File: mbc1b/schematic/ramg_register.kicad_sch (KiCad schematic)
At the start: 8 parts

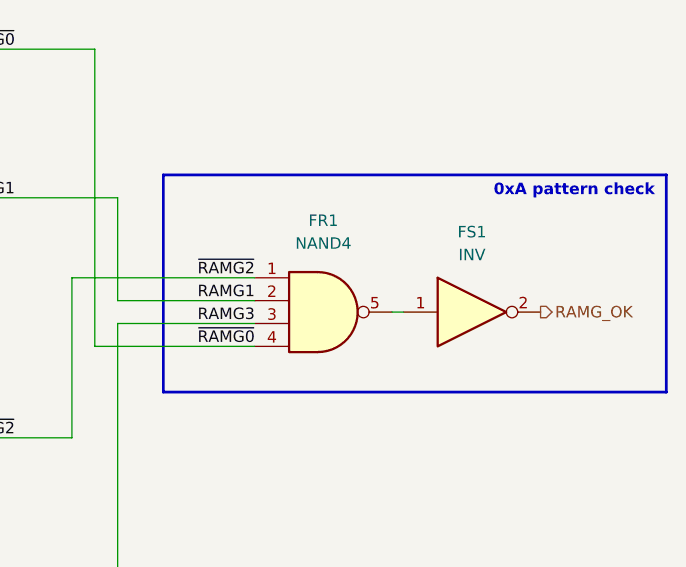
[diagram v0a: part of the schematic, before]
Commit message: Update MBC1B schematic with latest kingfish compatibility
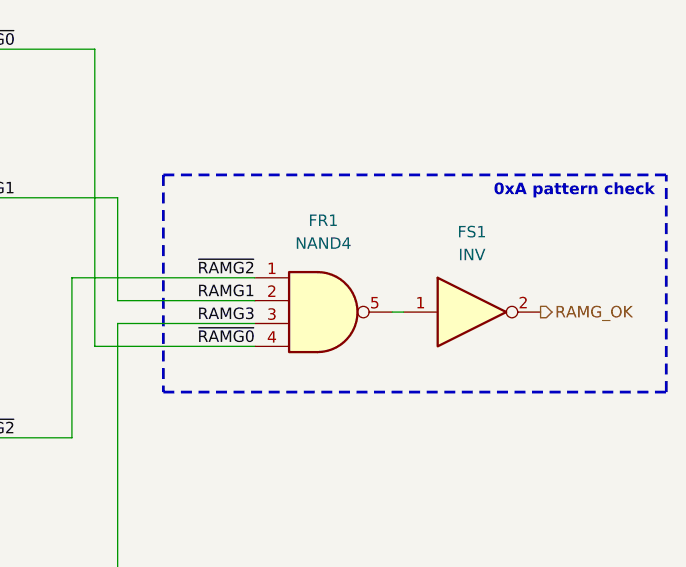
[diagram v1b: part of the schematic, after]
